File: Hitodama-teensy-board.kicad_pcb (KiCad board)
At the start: 2 copper layers, 5 parts, among them U4 Teensy3.6

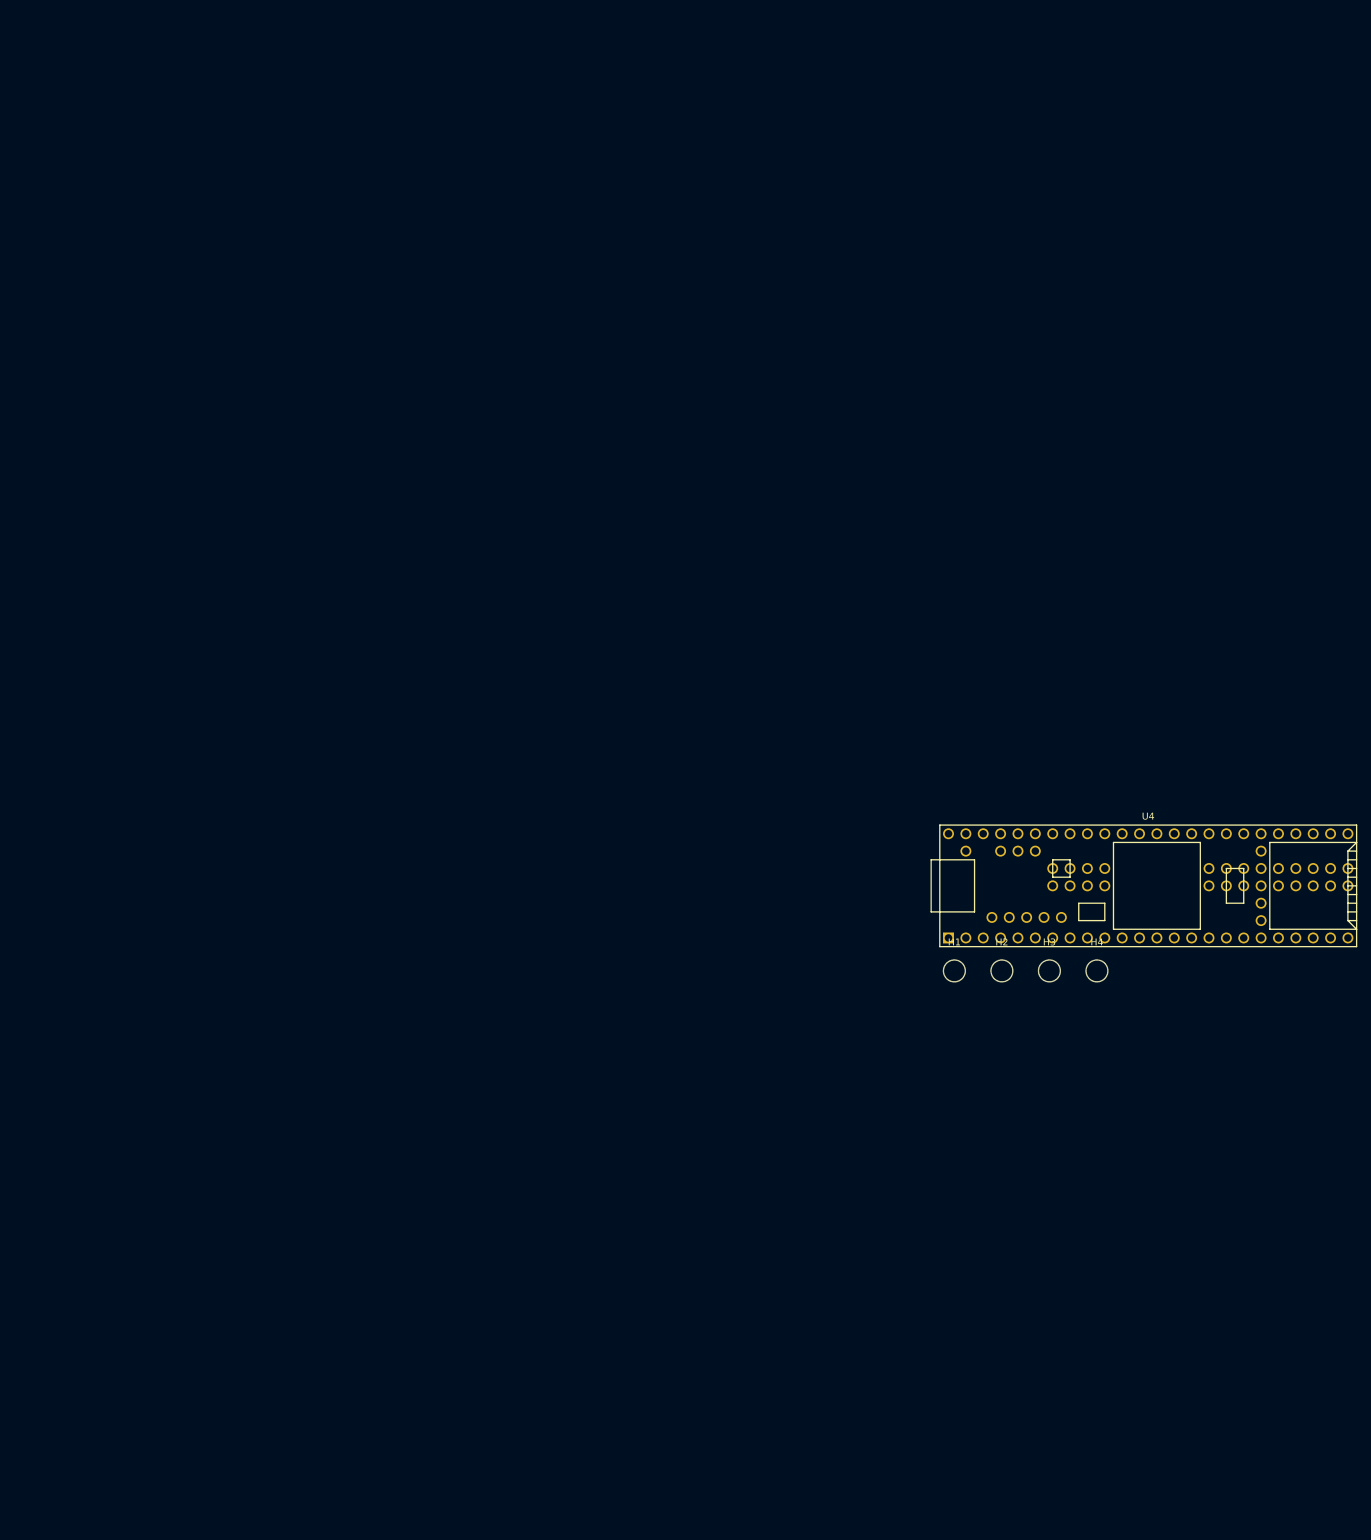
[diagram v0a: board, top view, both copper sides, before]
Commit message: Coordinate Connectors on both boards
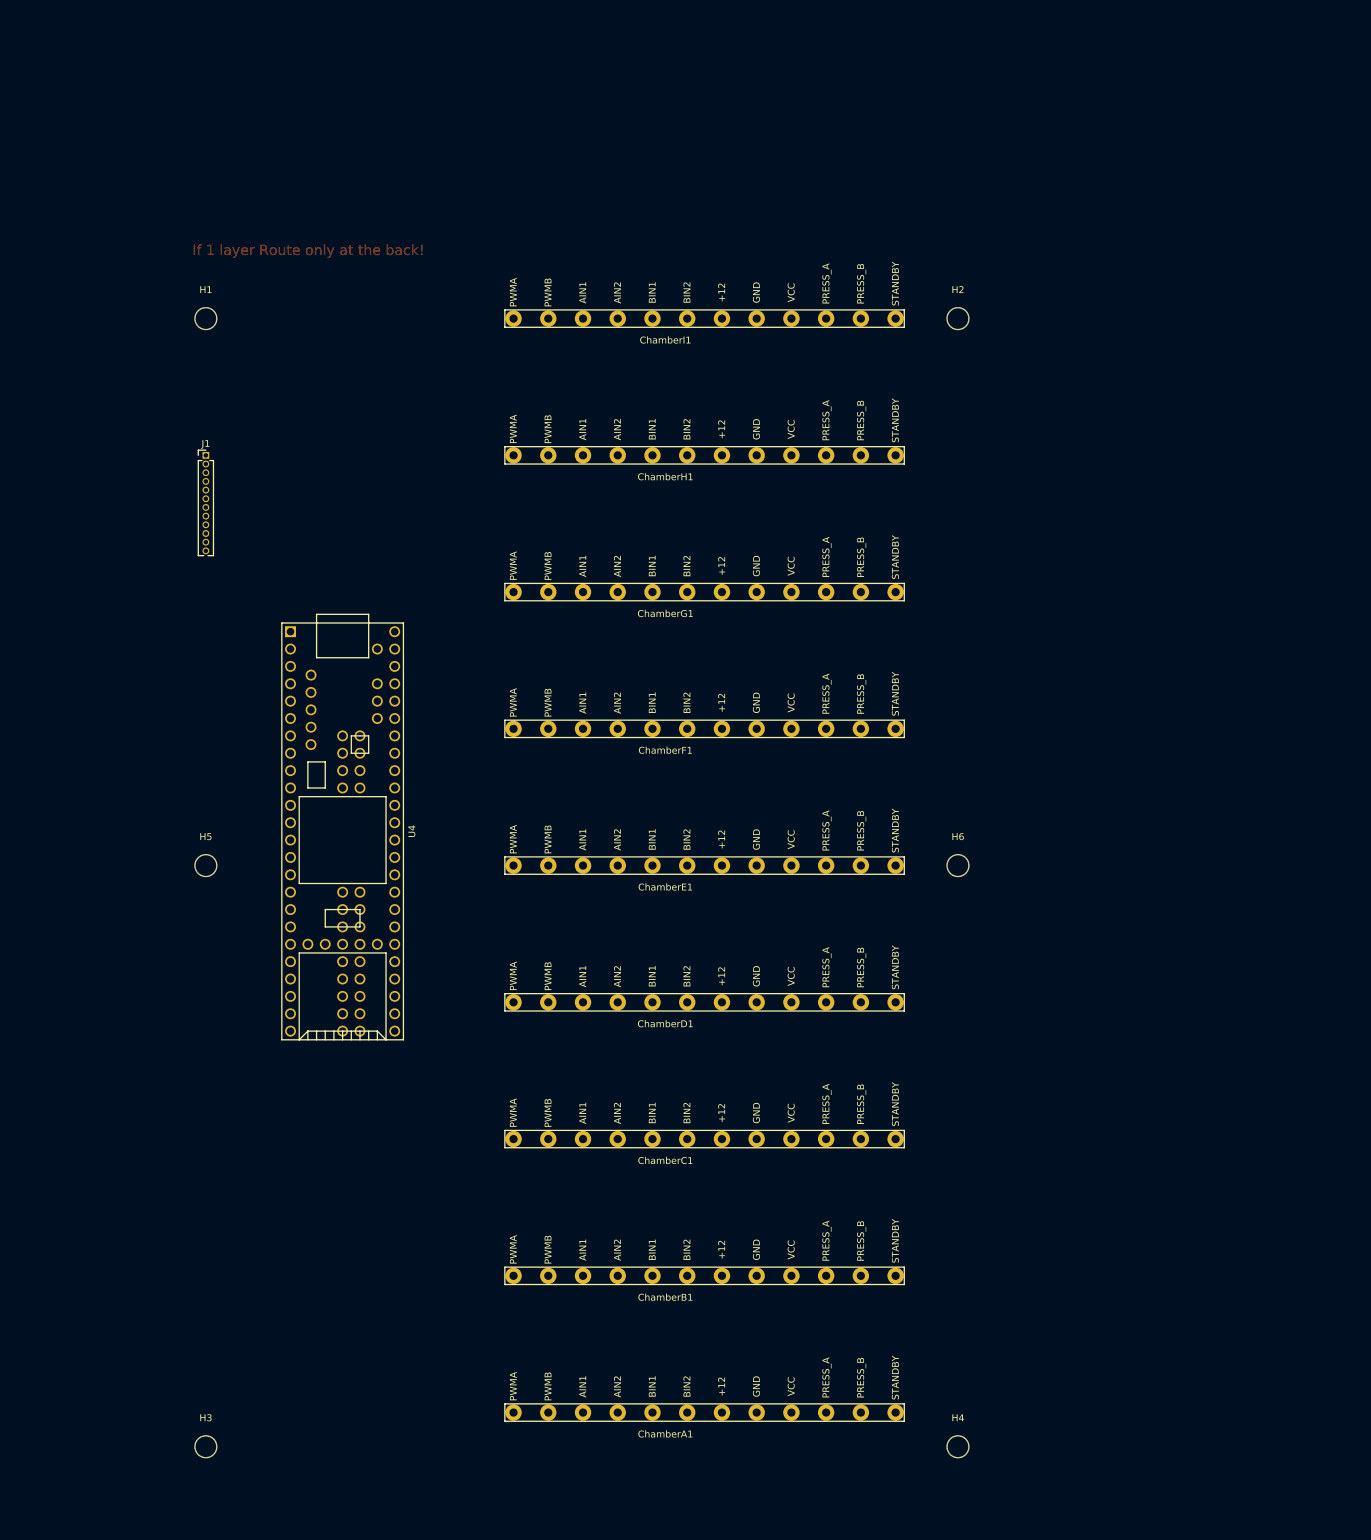
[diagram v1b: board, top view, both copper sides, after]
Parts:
- added ChamberA1: ChamberBoard_Holder, chamber_board_holder:chamber_board_holder, F.Cu at (60.0, 175.0)
- added ChamberB1: ChamberBoard_Holder, chamber_board_holder:chamber_board_holder, F.Cu at (60.0, 155.0)
- added ChamberC1: ChamberBoard_Holder, chamber_board_holder:chamber_board_holder, F.Cu at (60.0, 135.0)
- added ChamberD1: ChamberBoard_Holder, chamber_board_holder:chamber_board_holder, F.Cu at (60.0, 115.0)
- added ChamberE1: ChamberBoard_Holder, chamber_board_holder:chamber_board_holder, F.Cu at (60.0, 95.0)
- added ChamberF1: ChamberBoard_Holder, chamber_board_holder:chamber_board_holder, F.Cu at (60.0, 75.0)
- added ChamberG1: ChamberBoard_Holder, chamber_board_holder:chamber_board_holder, F.Cu at (60.0, 55.0)
- added ChamberH1: ChamberBoard_Holder, chamber_board_holder:chamber_board_holder, F.Cu at (60.0, 35.0)
- added ChamberI1: ChamberBoard_Holder, chamber_board_holder:chamber_board_holder, F.Cu at (60.0, 15.0)
- added H5: MountingHole, MountingHole:MountingHole_3.2mm_M3, F.Cu at (15.0, 95.0)
- added H6: MountingHole, MountingHole:MountingHole_3.2mm_M3, F.Cu at (125.0, 95.0)
- added J1: Conn_01x12_Male, Connector_PinHeader_1.27mm:PinHeader_1x12_P1.27mm_Vertical, F.Cu at (15.0, 35.0)
- moved H1 145.2 mm to (15.0, 15.0)
- moved H3 141.7 mm to (15.0, 180.0)
- moved U4 118.1 mm to (35.0, 90.0), turned to 270 degrees
- moved H2 95.6 mm to (125.0, 15.0)
- moved H4 72.5 mm to (125.0, 180.0)
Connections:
- net Net-(U4-Pad12) renamed /SPI0.CS0
- net Net-(U4-Pad13) renamed /SPI0.MOSI
- net Net-(U4-Pad14) renamed /SPI0.MISO
- net Net-(U4-Pad15) renamed +3V3
- net Net-(U4-Pad16) renamed /PanicBtn
- net Net-(U4-Pad40) renamed /SPI0.SCK
- U4 pad 10: Net-(U4-Pad10) -> /ChamberE.PWM
- U4 pad 11: Net-(U4-Pad11) -> /ChamberA.D2
- U4 pad 17: Net-(U4-Pad17) -> /All.Stby
- U4 pad 18: Net-(U4-Pad18) -> /ChamberA.D3
- U4 pad 19: Net-(U4-Pad19) -> /ChamberB.D1
- U4 pad 20: Net-(U4-Pad20) -> /ChamberB.D2
- U4 pad 21: Net-(U4-Pad21) -> /ChamberF.PWM
- U4 pad 22: Net-(U4-Pad22) -> /ChamberG.PWM
- U4 pad 23: Net-(U4-Pad23) -> /ChamberB.D3
- U4 pad 24: Net-(U4-Pad24) -> /ChamberC.D1
- U4 pad 30: Net-(U4-Pad30) -> /ChamberH.ADC
- U4 pad 31: Net-(U4-Pad31) -> /ChamberG.ADC
- U4 pad 32: Net-(U4-Pad32) -> /ChamberF.ADC
- U4 pad 33: Net-(U4-Pad33) -> /ChamberE.ADC
- U4 pad 34: Net-(U4-Pad34) -> /ChamberD.ADC
- U4 pad 35: Net-(U4-Pad35) -> /ChamberC.ADC
- U4 pad 36: Net-(U4-Pad36) -> /ChamberB.ADC
- U4 pad 37: Net-(U4-Pad37) -> /ChamberA.ADC
- U4 pad 38: Net-(U4-Pad38) -> /ChamberG.D2
- U4 pad 4: Net-(U4-Pad4) -> /ChamberC.PWM
- U4 pad 41: Net-(U4-Pad41) -> /ChamberG.D1
- U4 pad 42: Net-(U4-Pad42) -> /ChamberF.D3
- U4 pad 43: Net-(U4-Pad43) -> /ChamberF.D2
- U4 pad 44: Net-(U4-Pad44) -> /ChamberI.PWM
- U4 pad 45: Net-(U4-Pad45) -> /ChamberF.D1
- U4 pad 46: Net-(U4-Pad46) -> /ChamberE.D3
- U4 pad 47: Net-(U4-Pad47) -> /ChamberE.D2
- U4 pad 48: Net-(U4-Pad48) -> /ChamberE.D1
- U4 pad 49: Net-(U4-Pad49) -> /ChamberD.D3
- U4 pad 5: Net-(U4-Pad5) -> /ChamberH.PWM
- U4 pad 50: Net-(U4-Pad50) -> /ChamberD.D2
- U4 pad 56: Net-(U4-Pad56) -> /A10
- U4 pad 57: Net-(U4-Pad57) -> /A11
- U4 pad 6: Net-(U4-Pad6) -> /ChamberA.D1
- U4 pad 62: GND -> Net-(U4-Pad62)
- U4 pad 67: Net-(U4-Pad67) -> /ChamberC.D2
- U4 pad 68: Net-(U4-Pad68) -> /ChamberI.D2
- U4 pad 69: Net-(U4-Pad69) -> /ChamberI.D1
- U4 pad 7: Net-(U4-Pad7) -> /ChamberA.PWM
- U4 pad 70: Net-(U4-Pad70) -> /ChamberH.D3
- U4 pad 71: Net-(U4-Pad71) -> /ChamberH.D2
- U4 pad 72: Net-(U4-Pad72) -> /ChamberH.D1
- U4 pad 73: Net-(U4-Pad73) -> /ChamberG.D3
- U4 pad 76: Net-(U4-Pad76) -> /ChamberC.D3
- U4 pad 77: Net-(U4-Pad77) -> /ChamberD.D1
- U4 pad 78: Net-(U4-Pad78) -> /ChamberI.ADC
- U4 pad 79: Net-(U4-Pad79) -> /A24
- U4 pad 8: Net-(U4-Pad8) -> /ChamberB.PWM
- U4 pad 80: Net-(U4-Pad80) -> /D51
- U4 pad 81: Net-(U4-Pad81) -> /D52
- U4 pad 82: Net-(U4-Pad82) -> /D53
- U4 pad 83: Net-(U4-Pad83) -> /D54
- U4 pad 84: Net-(U4-Pad84) -> /ChamberI.D3
- U4 pad 85: Net-(U4-Pad85) -> /D56
- U4 pad 86: Net-(U4-Pad86) -> /D57
- U4 pad 9: Net-(U4-Pad9) -> /ChamberD.PWM
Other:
- board text added: "If 1 layer Route only at the back!"

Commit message: (auto) routing
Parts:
- removed J1: Conn_01x12_Male, Connector_PinHeader_1.27mm:PinHeader_1x12_P1.27mm_Vertical
- moved H1 1.41 mm to (14.0, 14.0)
- moved H2 1.00 mm to (125.0, 14.0)
- moved H3 1.00 mm to (14.0, 180.0)
- moved H5 1.00 mm to (14.0, 95.0)
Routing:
- net /All.Stby: track 0.00 -> 278.1 mm
- net VCC: track 0.00 -> 160.0 mm
- net +12V: track 0.00 -> 160.0 mm
- net /ChamberI.ADC: track 0.00 -> 125.4 mm
- net /ChamberA.D1: track 0.00 -> 121.8 mm
- net /ChamberA.PWM: track 0.00 -> 115.1 mm
- net /ChamberA.ADC: track 0.00 -> 113.7 mm, vias 0 -> 1
- net /ChamberH.ADC: track 0.00 -> 113.7 mm, vias 0 -> 1
- net /ChamberB.ADC: track 0.00 -> 112.5 mm
- net /ChamberA.D2: track 0.00 -> 110.8 mm
- net /ChamberH.D1: track 0.00 -> 107.2 mm
- net /ChamberI.D1: track 0.00 -> 105.4 mm
- net /ChamberI.D2: track 0.00 -> 103.9 mm
- net /ChamberA.D3: track 0.00 -> 100.6 mm
- net /ChamberH.D3: track 0.00 -> 96.7 mm
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- added copper zone on B.Cu, net GND
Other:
- board outline added: 119 x 174 mm
- net class Default: clearance 0.2 -> 0.31; trace_width 0.25 -> 0.31; via_dia 0.8 -> 2; via_drill 0.4 -> 1
- rule trace_clearance: 0.2 -> 0.31

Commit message: push some paths around
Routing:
- net /ChamberF.ADC: track 82.0 -> 85.7 mm
- net /ChamberH.ADC: track 113.7 -> 115.8 mm
- net /ChamberE.ADC: track 83.1 -> 81.1 mm
- net /ChamberG.ADC: track 91.0 -> 92.2 mm
- net /ChamberC.D2: track 62.1 -> 63.2 mm
- net /ChamberB.ADC: track 112.5 -> 111.5 mm
